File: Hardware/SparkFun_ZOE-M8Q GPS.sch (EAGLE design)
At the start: 32 parts, among them J4 U.FL, U1 UBLOX_ZOE_M8-0-10, Y1 32.768kHz

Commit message: Updates schematic frame to letter size, updates parts (see description)
* Battery part updated - replaces 100 Ohm series reistor with 3.3K
* IC part updated - better pin names on symbol
* Inductor part updated with better pads
* 8 Pin connector added - moves SDA and SCL to their own through hole
* Adds and fixes silk around design
* Adds thermals to ground pour
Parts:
- FRAME1: value FRAME-LEDGER -> FRAME-LETTER; device SparkFun-Aesthetics:FRAME-LEDGER -> SparkFun-Aesthetics:FRAME-LETTER
- J3: device SparkFun-Connectors:CONN_06NO_SILK_NO_POP -> SparkFun-Connectors:CONN_08NO_SILK_FEMALE_PTH
- L2: value 2.2UH_SHIELDED_INDUCTOR -> 2.2uH; device SparkFun-Coils:2.2UH_SHIELDED_INDUCTOR -> SparkFun-Coils:2.2μH_SHIELDED_INDUCTOR
- R1: value 100 -> 3.3k; device SparkFun-Resistors:100OHM-0603-1/10W-1% -> SparkFun-Resistors:3.3KOHM-0603-1/10W-1%
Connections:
- removed net INT: J5.1, U1.PI013/EXTINT
- new net !INT: J5.1, U1.PI013/!EXTINT
- net RESET: now also U1.!RESET; no longer U1.RESET_N
- net SAFEBOOT: now also U1.!SAFEBOOT; no longer U1.SAFEBOOT_N
- net SCL/CLK: now also J3.7; no longer J3.1
- net SDA/CS: now also J3.8; no longer J3.5
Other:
- note added: "Battery"
- note added: "Battery Initial Charge: 2.3-2.8V Battery Charge Rate: 1mA MAX Voff: 2.0V 72 hours charge time from 2.0-3.1V"
- note removed: "Super Capacitor"
- moved on the sheet: B1, C1, C2, C3, D1, D2, FB1, J1, J4, J5, JP1, JP2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

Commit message: Adds VCC range and i2C Address to schematic.
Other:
- note added: "I2C Address: 0x42"
- note added: "VCC Range: 1.89 - 3.6V"
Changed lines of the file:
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@@
 Voff: 2.0V
 72 hours charge time from 2.0-3.1V</text>
+<text x="33.02" y="167.64" size="2.032" layer="97" font="vector">VCC Range: 1.89 - 3.6V</text>
+<text x="96.52" y="154.94" size="2.032" layer="97" font="vector">I2C Address: 0x42</text>
 </plain>
 <instances>

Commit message: Removes some silk, changes version number, removes prototype gerber files
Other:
- note added: "v10"
- note removed: "v01"
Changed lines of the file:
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@@
 <sheet>
 <plain>
-<text x="238.76" y="7.62" size="2.54" layer="94" font="vector">v01</text>
+<text x="238.76" y="7.62" size="2.54" layer="94" font="vector">v10</text>
 <text x="167.64" y="10.16" size="2.54" layer="94" font="vector">Elias Santistevan</text>
 <text x="5.08" y="175.26" size="5.08" layer="94" font="vector" ratio="12">uBlox ZOE-M8Q-0-10</text>

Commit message: Adds silk to battery terminals, adds initial mAH text to battery section in schematic.
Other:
- note added: "*Battery Initial Charge: 2.3-2.8V *Intial Battery Capacity (maH): 800mAH or Greater *Battery Charge Rate: 1mA MAX *Voff: 2.0V *72 hours charge time from 2.0-3.1V"
- note removed: "Battery Initial Charge: 2.3-2.8V Battery Charge Rate: 1mA MAX Voff: 2.0V 72 hours charge time from 2.0-3.1V"
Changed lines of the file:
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@@
 <wire x1="68.58" y1="99.06" x2="68.58" y2="0" width="0.1524" layer="97" style="shortdash"/>
 <wire x1="129.54" y1="99.06" x2="129.54" y2="0" width="0.1524" layer="97" style="shortdash"/>
-<text x="35.56" y="60.96" size="1.27" layer="97" font="vector">Battery Initial Charge: 2.3-2.8V
-Battery Charge Rate: 1mA MAX
-Voff: 2.0V
-72 hours charge time from 2.0-3.1V</text>
+<text x="33.02" y="60.96" size="1.27" layer="97" font="vector">*Battery Initial Charge: 2.3-2.8V
+*Intial Battery Capacity (maH):
+    800mAH or Greater
+*Battery Charge Rate: 1mA MAX
+*Voff: 2.0V
+*72 hours charge time from 2.0-3.1V</text>
 <text x="33.02" y="167.64" size="2.032" layer="97" font="vector">VCC Range: 1.89 - 3.6V</text>
 <text x="96.52" y="154.94" size="2.032" layer="97" font="vector">I2C Address: 0x42</text>

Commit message: Adds no connect silk, fixes net labels that have active low pins
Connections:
- net RESET renamed !RESET
- net SAFEBOOT renamed !SAFEBOOT
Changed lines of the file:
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@@
 </segment>
 </net>
-<net name="SAFEBOOT" class="0">
+<net name="!SAFEBOOT" class="0">
 <segment>
 <pinref part="U1" gate="G$1" pin="!SAFEBOOT"/>
@@
 </segment>
 </net>
-<net name="RESET" class="0">
+<net name="!RESET" class="0">
 <segment>
 <pinref part="U1" gate="G$1" pin="!RESET"/>

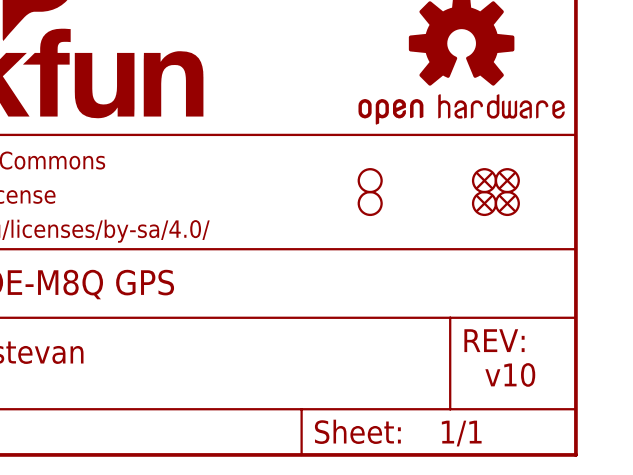
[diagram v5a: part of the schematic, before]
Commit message: Adds special ordering instructions and qwiic silk
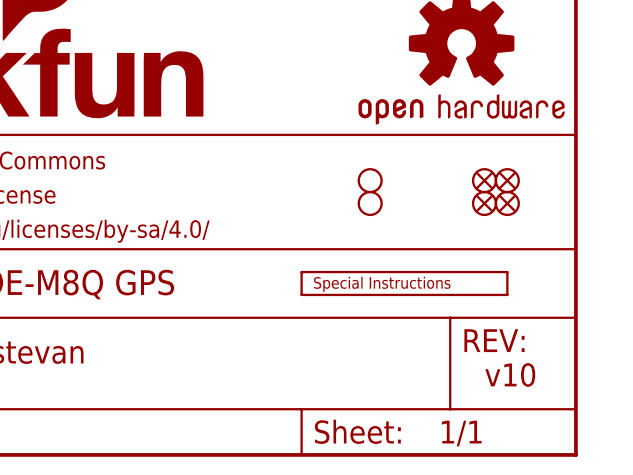
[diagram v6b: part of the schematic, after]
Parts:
- added LOGO4: SPECIAL_INSTRUCTIONS-ORDERING, SparkFun-Aesthetics:SPECIAL_INSTRUCTIONS-ORDERING
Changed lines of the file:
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@@
 <part name="C2" library="SparkFun-Capacitors" deviceset="0.1UF" device="-0603-25V-(+80/-20%)" value="0.1uF"/>
 <part name="FRAME1" library="SparkFun-Aesthetics" deviceset="FRAME-LETTER" device=""/>
+<part name="LOGO4" library="SparkFun-Aesthetics" deviceset="SPECIAL_INSTRUCTIONS" device="-ORDERING"/>
 </parts>
 <sheets>
@@
 <attribute name="REV" x="236.22" y="6.604" size="2.7432" layer="94" font="vector"/>
 </instance>
+<instance part="LOGO4" gate="G$1" x="218.44" y="17.78" smashed="yes"/>
 </instances>
 <busses>

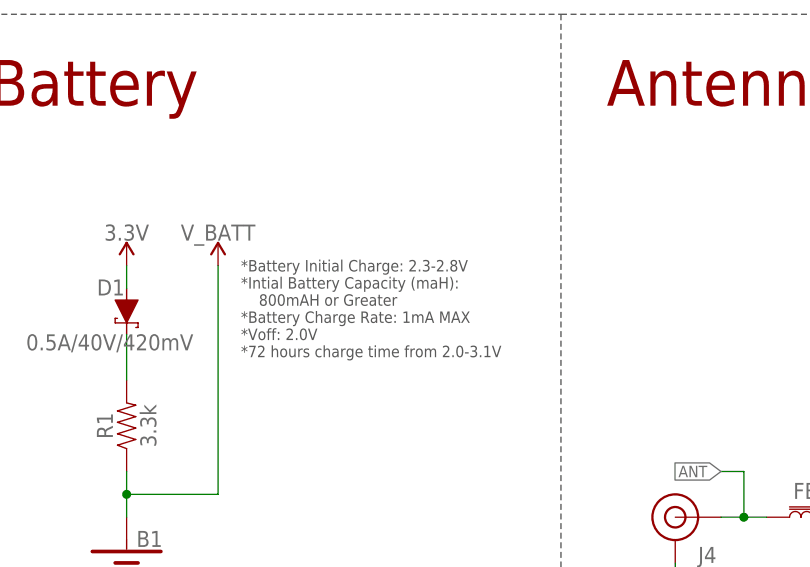
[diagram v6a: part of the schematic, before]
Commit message: Removes note about battery capacity that is entirely made up (erroneously of course).
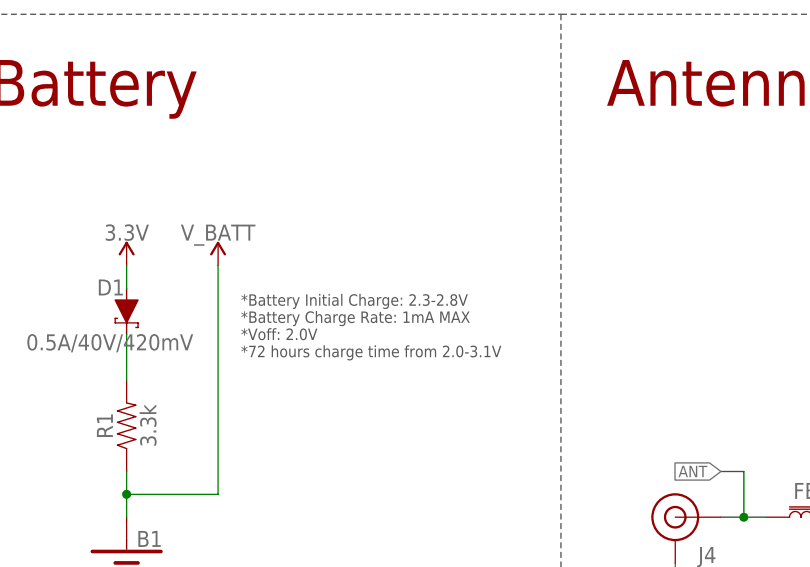
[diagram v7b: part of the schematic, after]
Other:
- note added: "*Battery Initial Charge: 2.3-2.8V *Battery Charge Rate: 1mA MAX *Voff: 2.0V *72 hours charge time from 2.0-3.1V"
- note removed: "*Battery Initial Charge: 2.3-2.8V *Intial Battery Capacity (maH): 800mAH or Greater *Battery Charge Rate: 1mA MAX *Voff: 2.0V *72 hours charge time from 2.0-3.1V"
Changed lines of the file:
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@@
 <?xml version="1.0" encoding="utf-8"?>
 <!DOCTYPE eagle SYSTEM "eagle.dtd">
-<eagle version="9.2.1">
+<eagle version="9.5.1">
 <drawing>
 <settings>
@@
 <wire x1="129.54" y1="99.06" x2="129.54" y2="0" width="0.1524" layer="97" style="shortdash"/>
 <text x="33.02" y="60.96" size="1.27" layer="97" font="vector">*Battery Initial Charge: 2.3-2.8V
-*Intial Battery Capacity (maH):
-    800mAH or Greater
 *Battery Charge Rate: 1mA MAX
 *Voff: 2.0V

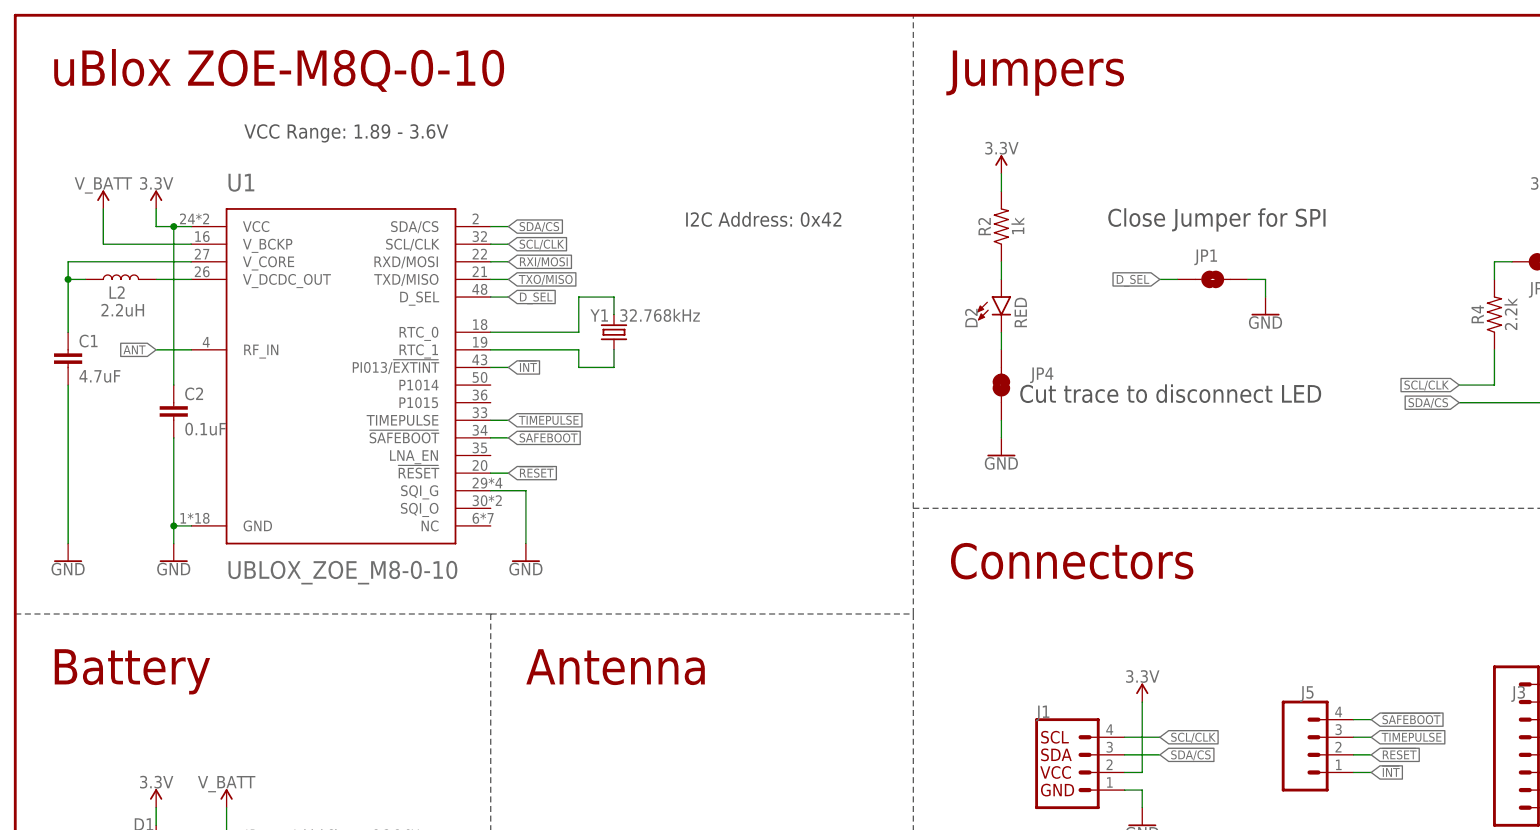
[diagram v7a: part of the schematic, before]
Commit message: Updates schematic
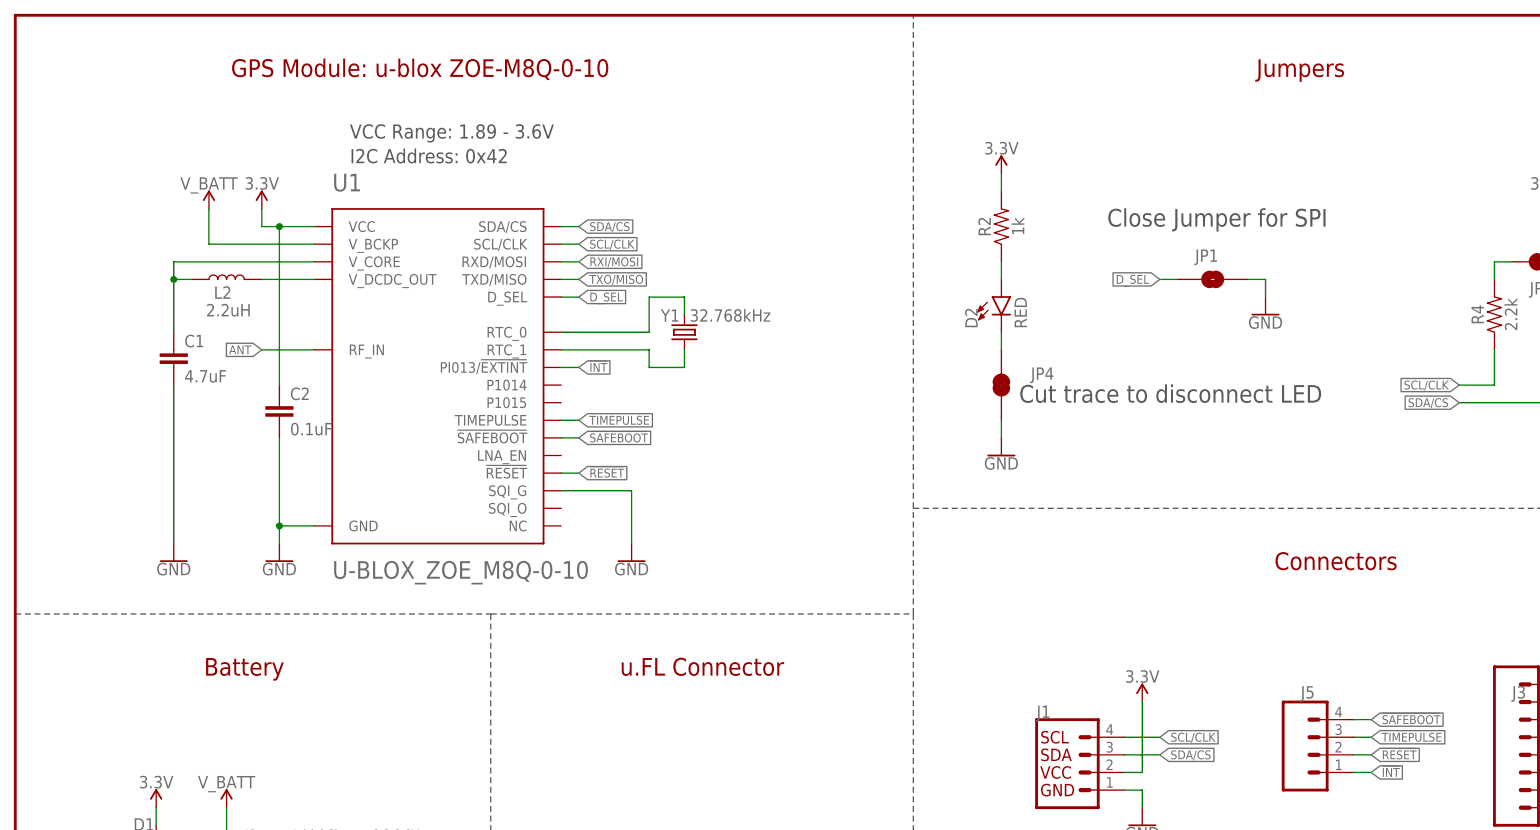
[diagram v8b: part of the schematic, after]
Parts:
- U1: value UBLOX_ZOE_M8-0-10 -> U-BLOX_ZOE_M8Q-0-10; device SparkFun-GPS:UBLOX_ZOE_M8-0-10 -> SparkFun-GPS:U-BLOX_ZOE_M8Q-0-10
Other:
- note added: "GPS Module: u-blox ZOE-M8Q-0-10"
- note added: "u.FL Connector"
- note removed: "Antenna"
- note removed: "uBlox ZOE-M8Q-0-10"
- moved on the sheet: C1, C2, L2, Y1
